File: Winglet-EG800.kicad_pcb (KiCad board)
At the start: 4 copper layers, 30 x 47.6 mm, 36 parts, among them J1 2337019-1, J2 NSIM-16-B, M1 PTH_M2.5, M2 PTH_M2.5, Q1 DMG1012UW-7, Q2 DMG1012UW-7, U1 FXLA108BQX, U2 EG800QEULC-N03-SNNSA, U3 MFF2-SIM, U4 24AA01T-I/OT

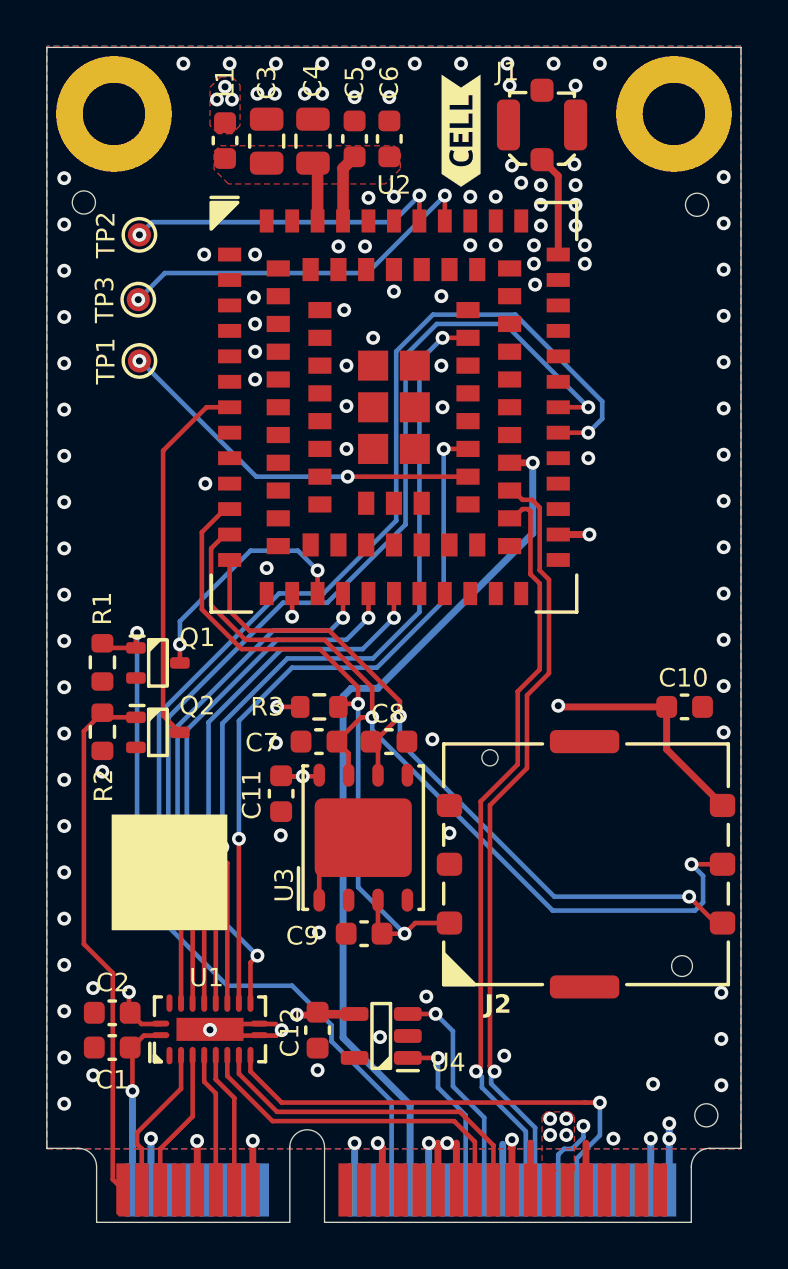
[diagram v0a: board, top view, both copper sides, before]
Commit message: Add test points. Finish layout
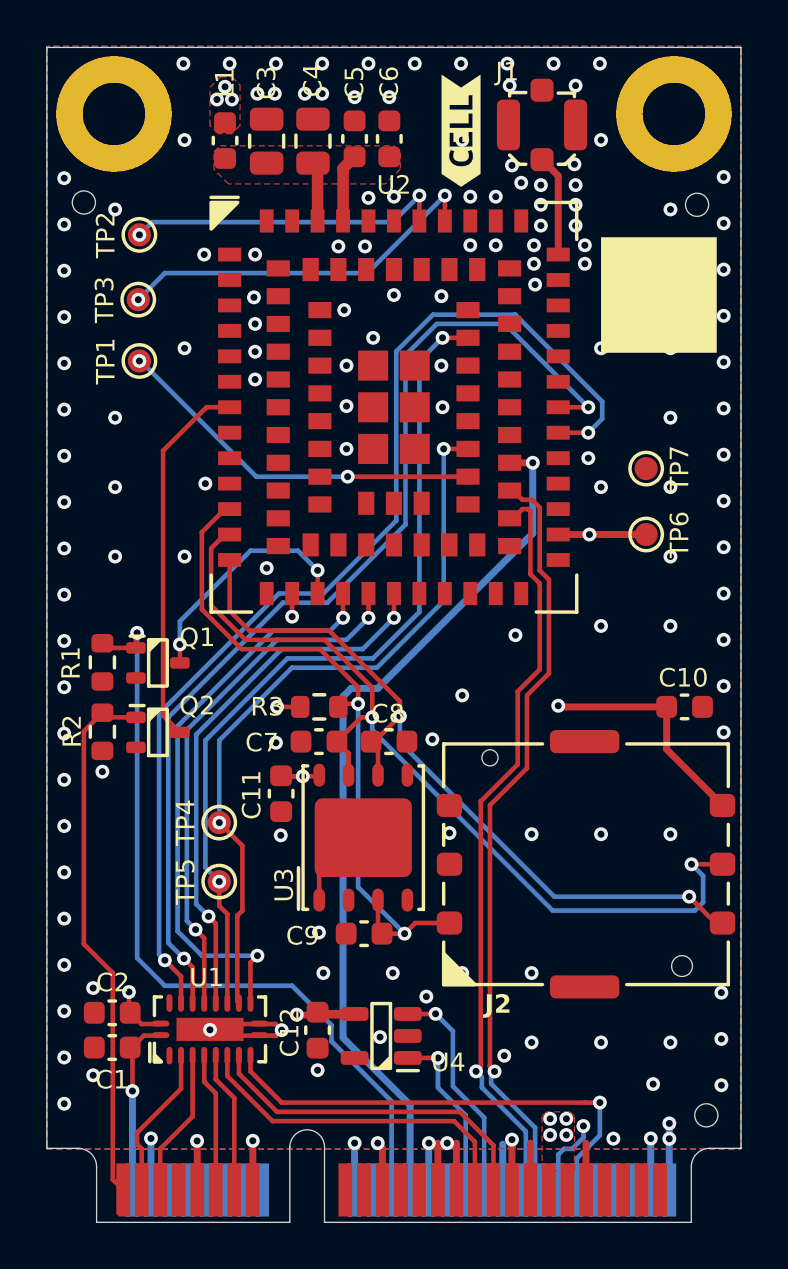
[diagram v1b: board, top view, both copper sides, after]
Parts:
- added TP4: ~, TP_TestPoint:TestPoint_1mm, F.Cu at (57.5, 83.5)
- added TP5: ~, TP_TestPoint:TestPoint_1mm, F.Cu at (57.5, 86.0)
- added TP6: ~, TP_TestPoint:TestPoint_1mm, F.Cu at (75.9, 71.0)
- added TP7: ~, TP_TestPoint:TestPoint_1mm, F.Cu at (75.9, 68.2)
- moved N1 32.7 mm to (76.5, 60.7)
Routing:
- net +1V8: track 38.2 -> 40.7 mm
- net /Connector/RESET: track 32.2 -> 33.8 mm
- net /Connector/MODEM_NETLIGHT: track 23.7 -> 25.1 mm
- net /Connector/MODEM_PSM_IND: track 30.8 -> 31.7 mm
- net /Connector/MODEM_PSM_INT: track 36.1 -> 36.7 mm
- net GND: vias 121 -> 152
